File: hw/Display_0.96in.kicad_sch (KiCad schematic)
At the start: 3 parts, among them J5 BM20B(0.8)-10DS-0.4V

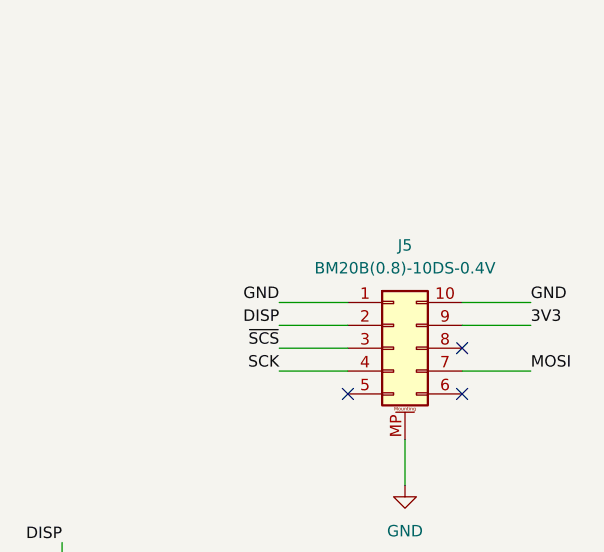
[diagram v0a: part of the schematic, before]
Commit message: fix footprint of BM20B(x)-10DS-0.4V
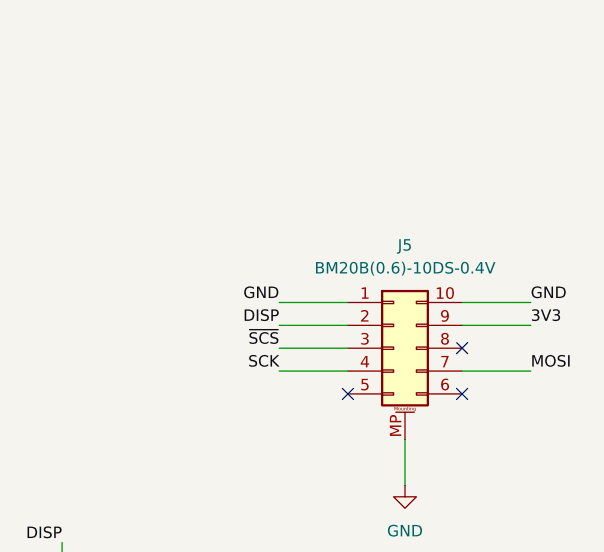
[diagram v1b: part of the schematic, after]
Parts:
- J5: value BM20B(0.8)-10DS-0.4V -> BM20B(0.6)-10DS-0.4V; footprint IotPi_Connector_Hirose:BM20B(0.8)-10DS-0.4V -> IotPi_Connector_Hirose:BM20B(x)-10DS-0.4V
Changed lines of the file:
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@@
       (effects (font (size 1.27 1.27)))
     )
-    (property "Value" "BM20B(0.8)-10DS-0.4V" (at 138.43 54.61 0)
+    (property "Value" "BM20B(0.6)-10DS-0.4V" (at 138.43 54.61 0)
       (effects (font (size 1.27 1.27)))
     )
-    (property "Footprint" "IotPi_Connector_Hirose:BM20B(0.8)-10DS-0.4V" (at 137.16 63.5 0)
+    (property "Footprint" "IotPi_Connector_Hirose:BM20B(x)-10DS-0.4V" (at 137.16 63.5 0)
       (effects (font (size 1.27 1.27)) hide)
     )

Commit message: updated Sheet and Board Information
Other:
- company: Qingdao IotPi Information Technology Ltd., -> Beijing Exponential Deep Space
- title: KiCad 2023 Shen Zhen Badge -> KiCad 2023 Asia Badge
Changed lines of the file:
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@@
   (paper "A4")
   (title_block
-    (title "KiCad 2023 Shen Zhen Badge")
-    (date "2023-10-04")
+    (title "KiCad 2023 Asia Badge")
+    (date "2023-10-07")
     (rev "2")
-    (company "Qingdao IotPi Information Technology Ltd.,")
+    (company "Beijing Exponential Deep Space")
     (comment 1 "Designed by Yang Hongbo")
   )

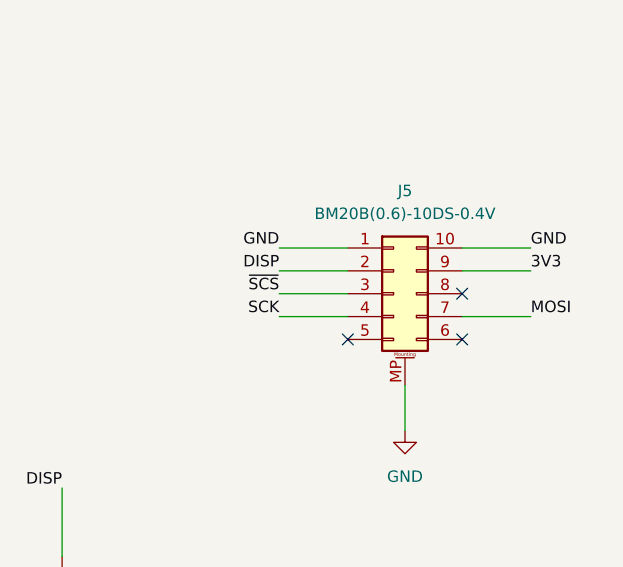
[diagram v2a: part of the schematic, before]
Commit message: fix JDI display connector pinout
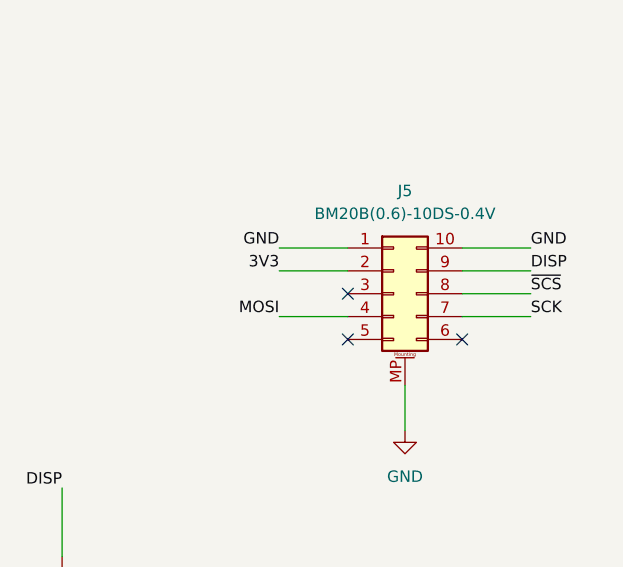
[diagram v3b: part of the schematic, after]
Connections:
- net 3V3: now also J5.2 (Pin_2); no longer J5.9 (Pin_9)
- net DISP: now also J5.9 (Pin_9); no longer J5.2 (Pin_2)
- net MOSI: now also J5.4 (Pin_4); no longer J5.7 (Pin_7)
- net SCK: now also J5.7 (Pin_7); no longer J5.4 (Pin_4)
- net ~{SCS}: now also J5.8 (Pin_8); no longer J5.3 (Pin_3)
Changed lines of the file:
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@@
     (comment 1 "Designed by Yang Hongbo")
   )
-  (no_connect (at 144.78 63.5))
+  (no_connect (at 132.08 63.5))
+  (no_connect (at 132.08 68.58))
   (no_connect (at 144.78 68.58))
-  (no_connect (at 132.08 68.58))
   (wire (pts (xy 38.1 39.37) (xy 46.99 39.37))
     (stroke (width 0) (type default))
   )
-  (wire (pts (xy 124.46 63.5) (xy 132.08 63.5))
+  (wire (pts (xy 152.4 63.5) (xy 144.78 63.5))
     (stroke (width 0) (type default))
   )
@@
     (stroke (width 0) (type default))
   )
-  (wire (pts (xy 124.46 58.42) (xy 132.08 58.42))
+  (wire (pts (xy 152.4 58.42) (xy 144.78 58.42))
     (stroke (width 0) (type default))
   )
-  (wire (pts (xy 144.78 58.42) (xy 152.4 58.42))
+  (wire (pts (xy 132.08 58.42) (xy 124.46 58.42))
     (stroke (width 0) (type default))
   )
-  (wire (pts (xy 124.46 60.96) (xy 132.08 60.96))
+  (wire (pts (xy 152.4 60.96) (xy 144.78 60.96))
     (stroke (width 0) (type default))
   )
-  (wire (pts (xy 144.78 60.96) (xy 152.4 60.96))
+  (wire (pts (xy 132.08 60.96) (xy 124.46 60.96))
     (stroke (width 0) (type default))
   )
-  (wire (pts (xy 144.78 66.04) (xy 152.4 66.04))
+  (wire (pts (xy 132.08 66.04) (xy 124.46 66.04))
     (stroke (width 0) (type default))
   )
@@
     (stroke (width 0) (type default))
   )
-  (wire (pts (xy 124.46 66.04) (xy 132.08 66.04))
+  (wire (pts (xy 152.4 66.04) (xy 144.78 66.04))
     (stroke (width 0) (type default))
   )
-  (label "~{SCS}" (at 124.46 63.5 180) (fields_autoplaced)
-    (effects (font (size 1.27 1.27)) (justify right bottom))
+  (label "~{SCS}" (at 152.4 63.5 0) (fields_autoplaced)
+    (effects (font (size 1.27 1.27)) (justify left bottom))
   )
   (label "DISP" (at 46.99 39.37 0) (fields_autoplaced)
     (effects (font (size 1.27 1.27)) (justify left bottom))
   )
-  (label "GND" (at 124.46 58.42 180) (fields_autoplaced)
-    (effects (font (size 1.27 1.27)) (justify right bottom))
+  (label "GND" (at 152.4 58.42 0) (fields_autoplaced)
+    (effects (font (size 1.27 1.27)) (justify left bottom))
   )
   (label "3V3" (at 46.99 29.21 0) (fields_autoplaced)
@@
     (effects (font (size 1.27 1.27)) (justify left bottom))
   )
-  (label "GND" (at 152.4 58.42 0) (fields_autoplaced)
-    (effects (font (size 1.27 1.27)) (justify left bottom))
+  (label "GND" (at 124.46 58.42 180) (fields_autoplaced)
+    (effects (font (size 1.27 1.27)) (justify right bottom))
   )
   (label "~{SCS}" (at 46.99 36.83 0) (fields_autoplaced)
@@
     (effects (font (size 1.27 1.27)) (justify right bottom))
   )
-  (label "DISP" (at 124.46 60.96 180) (fields_autoplaced)
+  (label "DISP" (at 152.4 60.96 0) (fields_autoplaced)
+    (effects (font (size 1.27 1.27)) (justify left bottom))
+  )
+  (label "SCK" (at 152.4 66.04 0) (fields_autoplaced)
+    (effects (font (size 1.27 1.27)) (justify left bottom))
+  )
+  (label "MOSI" (at 124.46 66.04 180) (fields_autoplaced)
     (effects (font (size 1.27 1.27)) (justify right bottom))
   )
-  (label "SCK" (at 124.46 66.04 180) (fields_autoplaced)
+  (label "3V3" (at 124.46 60.96 180) (fields_autoplaced)
     (effects (font (size 1.27 1.27)) (justify right bottom))
   )
-  (label "MOSI" (at 152.4 66.04 0) (fields_autoplaced)
-    (effects (font (size 1.27 1.27)) (justify left bottom))
-  )
-  (label "3V3" (at 152.4 60.96 0) (fields_autoplaced)
-    (effects (font (size 1.27 1.27)) (justify left bottom))
-  )
   (hierarchical_label "~{SCS}" (shape input) (at 38.1 36.83 180) (fields_autoplaced)

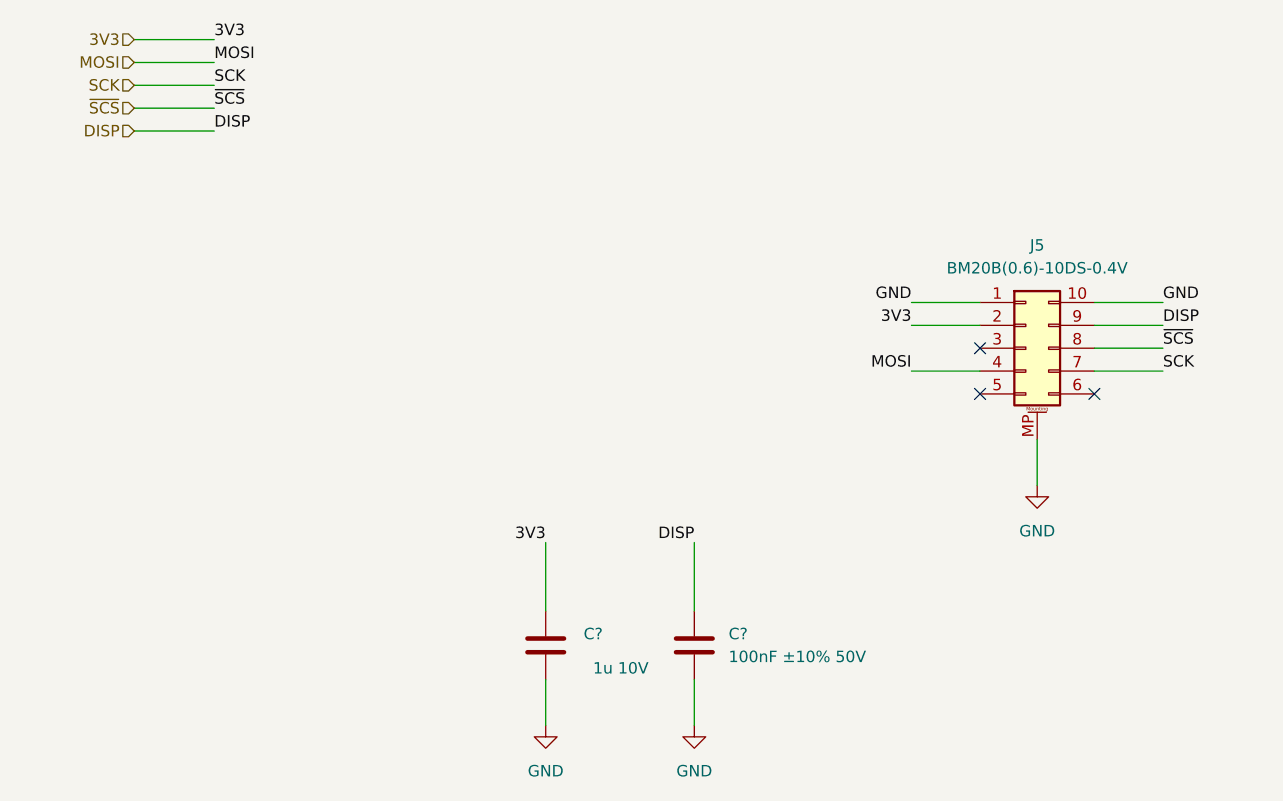
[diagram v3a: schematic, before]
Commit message: revert Display connector
fix SPI SS naming
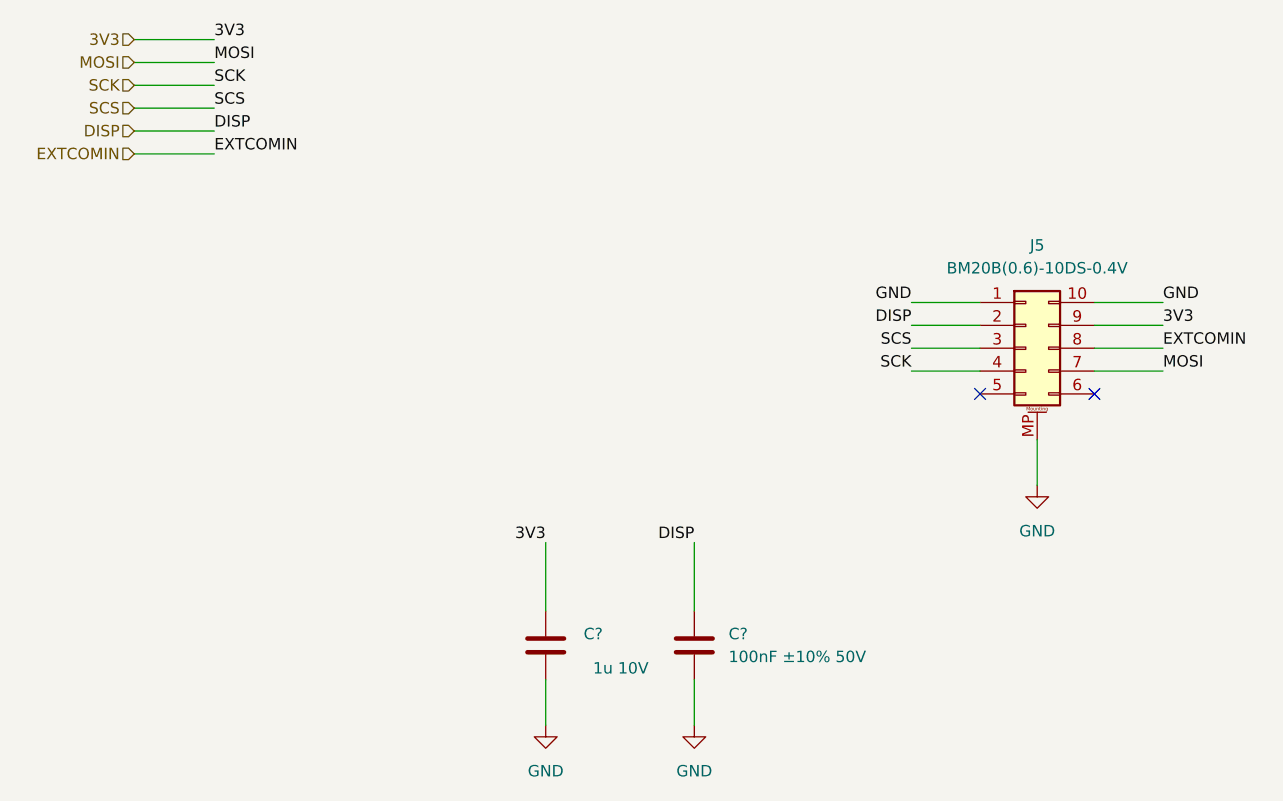
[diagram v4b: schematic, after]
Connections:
- net 3V3: now also J5.9 (Pin_9); no longer J5.2 (Pin_2)
- net DISP: now also J5.2 (Pin_2); no longer J5.9 (Pin_9)
- net MOSI: now also J5.7 (Pin_7); no longer J5.4 (Pin_4)
- net SCK: now also J5.4 (Pin_4); no longer J5.7 (Pin_7)
- net SCS: now reaches J5.3 (Pin_3)
- net ~{SCS} renamed EXTCOMIN
- no-connect marks 3 -> 2
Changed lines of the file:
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@@
     (comment 1 "Designed by Yang Hongbo")
   )
-  (no_connect (at 132.08 63.5))
   (no_connect (at 132.08 68.58))
   (no_connect (at 144.78 68.58))
@@
     (stroke (width 0) (type default))
   )
-  (wire (pts (xy 152.4 63.5) (xy 144.78 63.5))
+  (wire (pts (xy 124.46 63.5) (xy 132.08 63.5))
     (stroke (width 0) (type default))
   )
@@
     (stroke (width 0) (type default))
   )
-  (wire (pts (xy 152.4 58.42) (xy 144.78 58.42))
+  (wire (pts (xy 124.46 58.42) (xy 132.08 58.42))
     (stroke (width 0) (type default))
   )
-  (wire (pts (xy 132.08 58.42) (xy 124.46 58.42))
+  (wire (pts (xy 144.78 58.42) (xy 152.4 58.42))
     (stroke (width 0) (type default))
   )
-  (wire (pts (xy 152.4 60.96) (xy 144.78 60.96))
+  (wire (pts (xy 124.46 60.96) (xy 132.08 60.96))
     (stroke (width 0) (type default))
   )
-  (wire (pts (xy 132.08 60.96) (xy 124.46 60.96))
+  (wire (pts (xy 144.78 60.96) (xy 152.4 60.96))
     (stroke (width 0) (type default))
   )
-  (wire (pts (xy 132.08 66.04) (xy 124.46 66.04))
+  (wire (pts (xy 144.78 66.04) (xy 152.4 66.04))
     (stroke (width 0) (type default))
   )
@@
   )
   (wire (pts (xy 83.82 100.33) (xy 83.82 105.41))
+    (stroke (width 0) (type default))
+  )
+  (wire (pts (xy 38.1 41.91) (xy 46.99 41.91))
     (stroke (width 0) (type default))
   )
@@
     (stroke (width 0) (type default))
   )
-  (wire (pts (xy 152.4 66.04) (xy 144.78 66.04))
+  (wire (pts (xy 144.78 63.5) (xy 152.4 63.5))
     (stroke (width 0) (type default))
   )
-  (label "~{SCS}" (at 152.4 63.5 0) (fields_autoplaced)
-    (effects (font (size 1.27 1.27)) (justify left bottom))
+  (wire (pts (xy 124.46 66.04) (xy 132.08 66.04))
+    (stroke (width 0) (type default))
+  )
+  (label "SCS" (at 124.46 63.5 180) (fields_autoplaced)
+    (effects (font (size 1.27 1.27)) (justify right bottom))
   )
   (label "DISP" (at 46.99 39.37 0) (fields_autoplaced)
     (effects (font (size 1.27 1.27)) (justify left bottom))
   )
-  (label "GND" (at 152.4 58.42 0) (fields_autoplaced)
+  (label "GND" (at 124.46 58.42 180) (fields_autoplaced)
+    (effects (font (size 1.27 1.27)) (justify right bottom))
+  )
+  (label "3V3" (at 46.99 29.21 0) (fields_autoplaced)
     (effects (font (size 1.27 1.27)) (justify left bottom))
   )
-  (label "3V3" (at 46.99 29.21 0) (fields_autoplaced)
+  (label "EXTCOMIN" (at 152.4 63.5 0) (fields_autoplaced)
     (effects (font (size 1.27 1.27)) (justify left bottom))
   )
@@
     (effects (font (size 1.27 1.27)) (justify left bottom))
   )
-  (label "GND" (at 124.46 58.42 180) (fields_autoplaced)
-    (effects (font (size 1.27 1.27)) (justify right bottom))
+  (label "GND" (at 152.4 58.42 0) (fields_autoplaced)
+    (effects (font (size 1.27 1.27)) (justify left bottom))
   )
-  (label "~{SCS}" (at 46.99 36.83 0) (fields_autoplaced)
+  (label "SCS" (at 46.99 36.83 0) (fields_autoplaced)
     (effects (font (size 1.27 1.27)) (justify left bottom))
   )
@@
     (effects (font (size 1.27 1.27)) (justify right bottom))
   )
-  (label "DISP" (at 152.4 60.96 0) (fields_autoplaced)
+  (label "EXTCOMIN" (at 46.99 41.91 0) (fields_autoplaced)
     (effects (font (size 1.27 1.27)) (justify left bottom))
   )
-  (label "SCK" (at 152.4 66.04 0) (fields_autoplaced)
+  (label "DISP" (at 124.46 60.96 180) (fields_autoplaced)
+    (effects (font (size 1.27 1.27)) (justify right bottom))
+  )
+  (label "SCK" (at 124.46 66.04 180) (fields_autoplaced)
+    (effects (font (size 1.27 1.27)) (justify right bottom))
+  )
+  (label "MOSI" (at 152.4 66.04 0) (fields_autoplaced)
     (effects (font (size 1.27 1.27)) (justify left bottom))
   )
-  (label "MOSI" (at 124.46 66.04 180) (fields_autoplaced)
-    (effects (font (size 1.27 1.27)) (justify right bottom))
+  (label "3V3" (at 152.4 60.96 0) (fields_autoplaced)
+    (effects (font (size 1.27 1.27)) (justify left bottom))
   )
-  (label "3V3" (at 124.46 60.96 180) (fields_autoplaced)
-    (effects (font (size 1.27 1.27)) (justify right bottom))
-  )
-  (hierarchical_label "~{SCS}" (shape input) (at 38.1 36.83 180) (fields_autoplaced)
+  (hierarchical_label "SCS" (shape input) (at 38.1 36.83 180) (fields_autoplaced)
     (effects (font (size 1.27 1.27)) (justify right))
   )
@@
     (effects (font (size 1.27 1.27)) (justify right))
   )
+  (hierarchical_label "EXTCOMIN" (shape input) (at 38.1 41.91 180) (fields_autoplaced)
+    (effects (font (size 1.27 1.27)) (justify right))
+  )

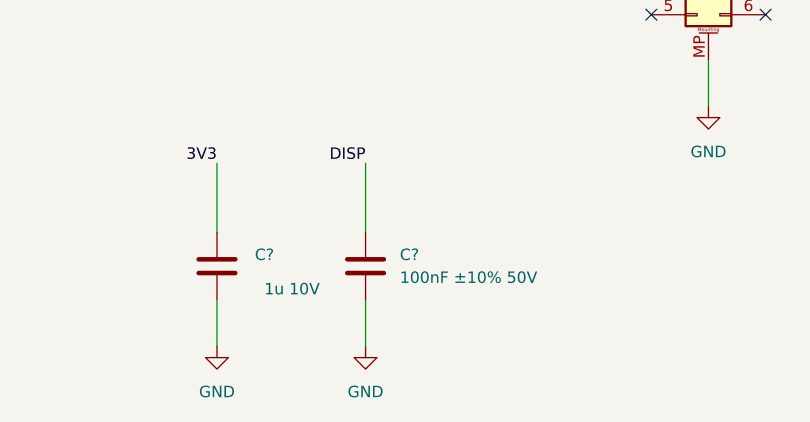
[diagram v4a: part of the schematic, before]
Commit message: fix Display Connector
and replace capacitors to 0402 size
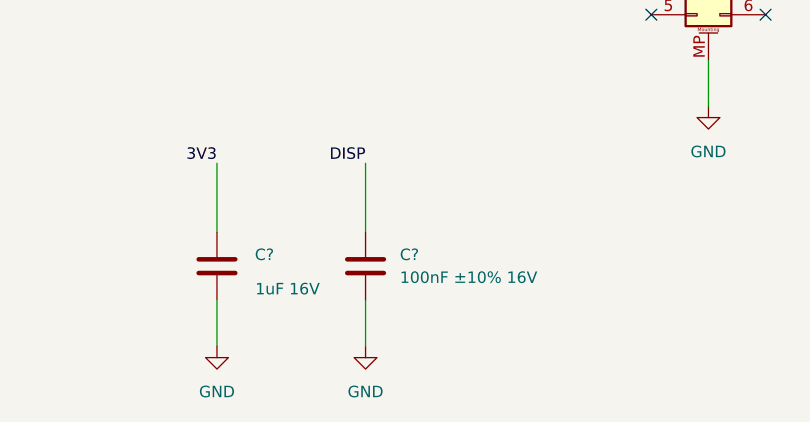
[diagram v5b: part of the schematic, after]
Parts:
- C?: value 100nF ±10% 50V -> 100nF ±10% 16V; footprint Capacitor_SMD:C_0805_2012Metric_Pad1.18x1.45mm_HandSolder -> Capacitor_SMD:C_0402_1005Metric; LCSC C49678 -> C1525; Vendor YAGEO(国巨) -> SAMSUNG(三星); Vendor Model CC0805KRX7R9BB104 -> CL05B104KO5NNNC
- C?: value 1u 10V -> 1uF 16V; footprint Resistor_SMD:R_0805_2012Metric_Pad1.20x1.40mm_HandSolder -> Resistor_SMD:R_0402_1005Metric; LCSC C28323 -> C52923; Vendor Model CL21B105KBFNNNE -> CL05A105KA5NQNC
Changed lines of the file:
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@@
       (effects (font (size 1.27 1.27)) (justify left))
     )
-    (property "Value" "100nF ±10% 50V" (at 104.14 97.79 0)
+    (property "Value" "100nF ±10% 16V" (at 104.14 97.79 0)
       (effects (font (size 1.27 1.27)) (justify left))
     )
-    (property "Footprint" "Capacitor_SMD:C_0805_2012Metric_Pad1.18x1.45mm_HandSolder" (at 101.2952 100.33 0)
+    (property "Footprint" "Capacitor_SMD:C_0402_1005Metric" (at 101.2952 100.33 0)
       (effects (font (size 1.27 1.27)) hide)
     )
@@
       (effects (font (size 1.27 1.27)) hide)
     )
-    (property "Description" "容值: 100nF 精度: ±5% 额定电压: 100V 材质(温度系数): X7R " (at 100.33 96.52 0)
+    (property "Description" "容值: 100nF 精度: ±10% 额定电压: 16V 材质(温度系数): X7R 材质:X7R" (at 100.33 96.52 0)
       (effects (font (size 1.27 1.27)) hide)
     )
-    (property "LCSC" "C49678" (at 100.33 96.52 0)
+    (property "LCSC" "C1525" (at 100.33 96.52 0)
       (effects (font (size 1.27 1.27)) hide)
     )
-    (property "Vendor" "YAGEO(国巨)" (at 100.33 96.52 0)
+    (property "Vendor" "SAMSUNG(三星)" (at 100.33 96.52 0)
       (effects (font (size 1.27 1.27)) hide)
     )
-    (property "Vendor Model" "CC0805KRX7R9BB104" (at 100.33 96.52 0)
+    (property "Vendor Model" "CL05B104KO5NNNC" (at 100.33 96.52 0)
       (effects (font (size 1.27 1.27)) hide)
     )
@@
       (effects (font (size 1.27 1.27)) (justify left))
     )
-    (property "Value" "1u 10V" (at 95.25 99.06 0)
+    (property "Value" "1uF 16V" (at 95.25 99.06 0)
       (effects (font (size 1.27 1.27)) (justify left))
     )
-    (property "Footprint" "Resistor_SMD:R_0805_2012Metric_Pad1.20x1.40mm_HandSolder" (at 82.8548 100.33 0)
+    (property "Footprint" "Resistor_SMD:R_0402_1005Metric" (at 82.8548 100.33 0)
       (effects (font (size 1.27 1.27)) hide)
     )
@@
       (effects (font (size 1.27 1.27)) hide)
     )
-    (property "Description" "容值: 1uF 精度: ±10% 额定电压: 50V 材质(温度系数): X7R 材质:X7R" (at 83.82 96.52 0)
+    (property "Description" "容值: 1uF 精度: ±10% 额定电压: 25V 材质(温度系数): X5R 材质:X5R" (at 83.82 96.52 0)
       (effects (font (size 1.27 1.27)) hide)
     )
-    (property "LCSC" "C28323" (at 83.82 96.52 0)
+    (property "LCSC" "C52923" (at 83.82 96.52 0)
       (effects (font (size 1.27 1.27)) hide)
     )
@@
       (effects (font (size 1.27 1.27)) hide)
     )
-    (property "Vendor Model" "CL21B105KBFNNNE" (at 83.82 96.52 0)
+    (property "Vendor Model" "CL05A105KA5NQNC" (at 83.82 96.52 0)
       (effects (font (size 1.27 1.27)) hide)
     )
